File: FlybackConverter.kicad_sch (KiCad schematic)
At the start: 42 parts, among them J1 USB_C_Receptacle_PowerOnly_6P, T1 Transformer_1P_2S, U1 LNK6428K, U2 TPS25820DSST

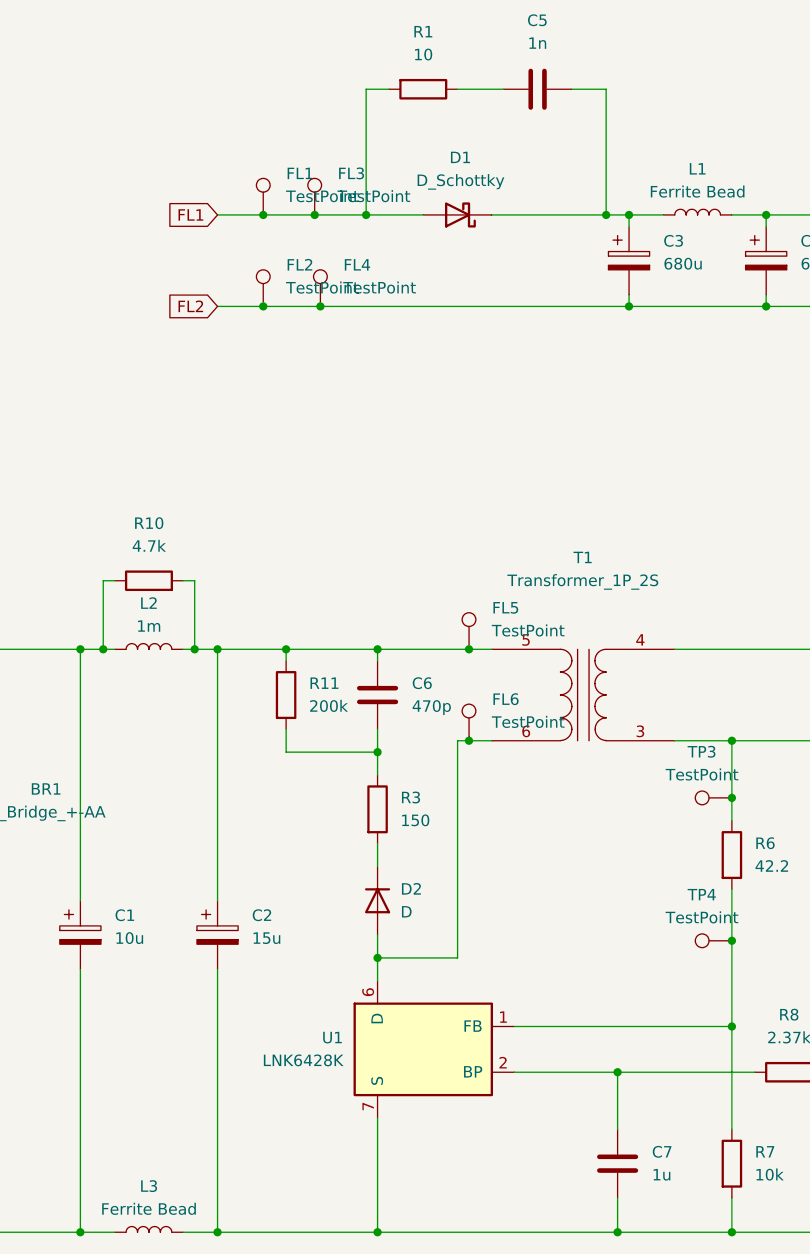
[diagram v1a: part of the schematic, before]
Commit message: トランスのフットプリントを10pinに修正
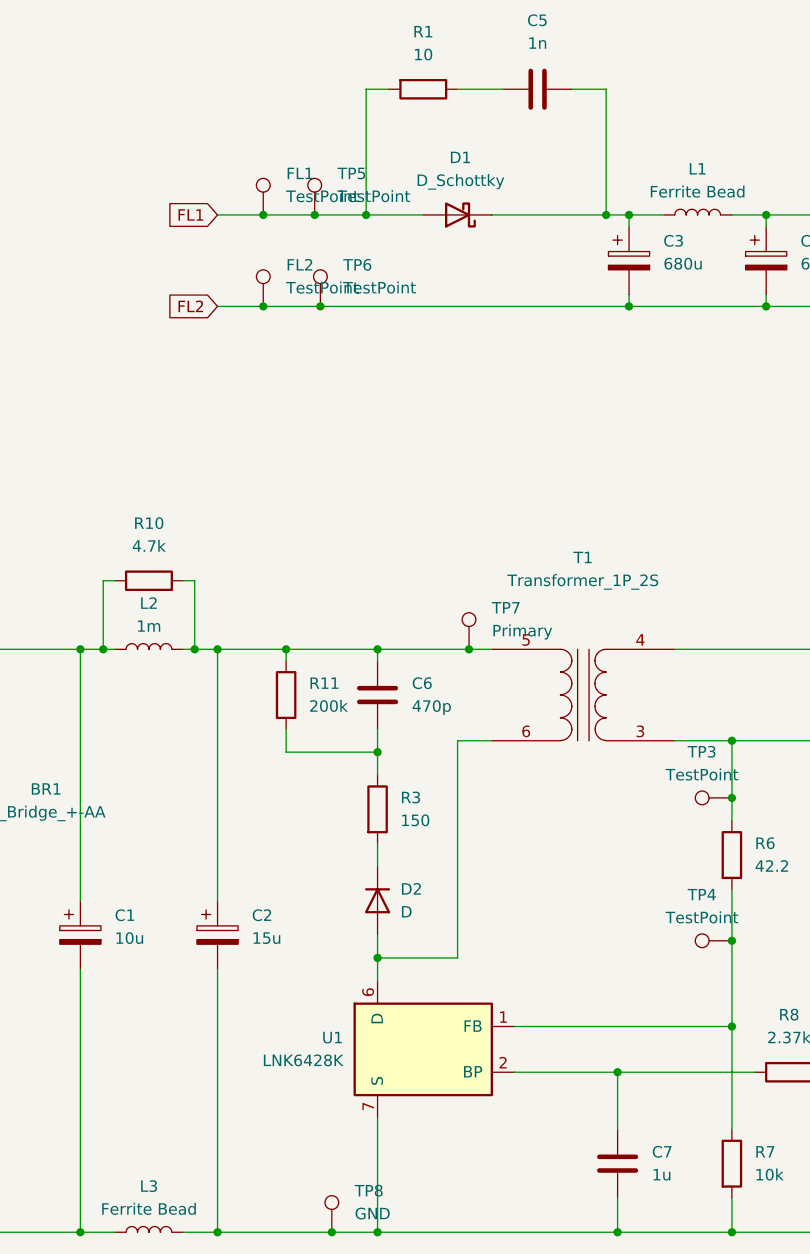
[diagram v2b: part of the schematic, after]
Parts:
- removed FL6: TestPoint, TestPoint:TestPoint_Loop_D1.80mm_Drill1.0mm_Beaded, symbol Connector:TestPoint
- added TP8: GND, TestPoint:TestPoint_Loop_D1.80mm_Drill1.0mm_Beaded, symbol Connector:TestPoint
- T1: footprint Transformer_THT:Transformer_CHK_EI38-3VA_2xSec -> 00_Library:BEPC17-1110CPHFR
- TP7: renamed from FL5; value TestPoint -> Primary
- renumbered FL3 to TP5, FL4 to TP6
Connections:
- net at C2.2, C7.2, C8.2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: now also TP8.1
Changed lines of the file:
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@@
   (junction (at 67.31 96.52) (diameter 0) (color 0 0 0 0)
   )
-  (junction (at 107.95 106.68) (diameter 0) (color 0 0 0 0)
-  )
   (junction (at 124.46 161.29) (diameter 0) (color 0 0 0 0)
   )
@@
   (junction (at 168.91 46.99) (diameter 0) (color 0 0 0 0)
   )
+  (junction (at 92.71 161.29) (diameter 0) (color 0 0 0 0)
+  )
   (junction (at 80.01 96.52) (diameter 0) (color 0 0 0 0)
   )
@@
     (stroke (width 0) (type default))
   )
-  (wire (pts (xy 106.68 106.68) (xy 107.95 106.68))
-    (stroke (width 0) (type default))
-  )
   (wire (pts (xy 97.79 105.41) (xy 97.79 107.95))
     (stroke (width 0) (type default))
@@
     (stroke (width 0) (type default))
   )
+  (wire (pts (xy 92.71 161.29) (xy 97.79 161.29))
+    (stroke (width 0) (type default))
+  )
   (wire (pts (xy 46.99 161.29) (xy 64.77 161.29))
     (stroke (width 0) (type default))
@@
     (stroke (width 0) (type default))
   )
-  (wire (pts (xy 107.95 106.68) (xy 110.49 106.68))
+  (wire (pts (xy 106.68 106.68) (xy 110.49 106.68))
     (stroke (width 0) (type default))
   )
@@
     (stroke (width 0) (type default))
   )
-  (wire (pts (xy 80.01 161.29) (xy 97.79 161.29))
+  (wire (pts (xy 80.01 161.29) (xy 92.71 161.29))
     (stroke (width 0) (type default))
   )
@@
     )
   )
-  (symbol (lib_id "Connector:TestPoint") (at 107.95 106.68 0) (unit 1)
-    (in_bom yes) (on_board yes) (dnp no) (fields_autoplaced)
-    (property "Reference" "FL6" (at 110.49 102.108 0)
-      (effects (font (size 1.27 1.27)) (justify left))
-    )
-    (property "Value" "TestPoint" (at 110.49 104.648 0)
-      (effects (font (size 1.27 1.27)) (justify left))
-    )
-    (property "Footprint" "TestPoint:TestPoint_Loop_D1.80mm_Drill1.0mm_Beaded" (at 113.03 106.68 0)
-      (effects (font (size 1.27 1.27)) hide)
-    )
-    (property "Datasheet" "~" (at 113.03 106.68 0)
-      (effects (font (size 1.27 1.27)) hide)
-    )
-    (pin "1")
-    (instances
-      (project "FlybackConverter"
-        (path "/f7ad8aa8-e3ae-4e7c-846c-9c0c6caa5ffd"
-          (reference "FL6") (unit 1)
-        )
-      )
-    )
-  )
   (symbol (lib_id "Device:R") (at 72.39 88.9 90) (unit 1)
     (in_bom yes) (on_board yes) (dnp no) (fields_autoplaced)
@@
     )
   )
+  (symbol (lib_id "Connector:TestPoint") (at 92.71 161.29 0) (unit 1)
+    (in_bom yes) (on_board yes) (dnp no) (fields_autoplaced)
+    (property "Reference" "TP8" (at 95.25 156.718 0)
+      (effects (font (size 1.27 1.27)) (justify left))
+    )
+    (property "Value" "GND" (at 95.25 159.258 0)
+      (effects (font (size 1.27 1.27)) (justify left))
+    )
+    (property "Footprint" "TestPoint:TestPoint_Loop_D1.80mm_Drill1.0mm_Beaded" (at 97.79 161.29 0)
+      (effects (font (size 1.27 1.27)) hide)
+    )
+    (property "Datasheet" "~" (at 97.79 161.29 0)
+      (effects (font (size 1.27 1.27)) hide)
+    )
+    (pin "1")
+    (instances
+      (project "FlybackConverter"
+        (path "/f7ad8aa8-e3ae-4e7c-846c-9c0c6caa5ffd"
+          (reference "TP8") (unit 1)
+        )
+      )
+    )
+  )
   (symbol (lib_id "Connector:TestPoint") (at 34.29 138.43 180) (unit 1)
     (in_bom yes) (on_board yes) (dnp no) (fields_autoplaced)
@@
   (symbol (lib_id "Connector:TestPoint") (at 90.805 48.26 0) (unit 1)
     (in_bom yes) (on_board yes) (dnp no) (fields_autoplaced)
-    (property "Reference" "FL3" (at 93.345 43.688 0)
+    (property "Reference" "TP5" (at 93.345 43.688 0)
       (effects (font (size 1.27 1.27)) (justify left))
     )
@@
       (project "FlybackConverter"
         (path "/f7ad8aa8-e3ae-4e7c-846c-9c0c6caa5ffd"
-          (reference "FL3") (unit 1)
+          (reference "TP5") (unit 1)
         )
       )
@@
       (effects (font (size 1.27 1.27)))
     )
-    (property "Footprint" "Transformer_THT:Transformer_CHK_EI38-3VA_2xSec" (at 120.65 101.6 0)
+    (property "Footprint" "00_Library:BEPC17-1110CPHFR" (at 120.65 101.6 0)
       (effects (font (size 1.27 1.27)) hide)
     )
@@
   (symbol (lib_id "Connector:TestPoint") (at 91.44 58.42 0) (unit 1)
     (in_bom yes) (on_board yes) (dnp no) (fields_autoplaced)
-    (property "Reference" "FL4" (at 93.98 53.848 0)
+    (property "Reference" "TP6" (at 93.98 53.848 0)
       (effects (font (size 1.27 1.27)) (justify left))
     )
@@
       (project "FlybackConverter"
         (path "/f7ad8aa8-e3ae-4e7c-846c-9c0c6caa5ffd"
-          (reference "FL4") (unit 1)
+          (reference "TP6") (unit 1)
         )
       )
@@
   (symbol (lib_id "Connector:TestPoint") (at 107.95 96.52 0) (unit 1)
     (in_bom yes) (on_board yes) (dnp no) (fields_autoplaced)
-    (property "Reference" "FL5" (at 110.49 91.948 0)
-      (effects (font (size 1.27 1.27)) (justify left))
-    )
-    (property "Value" "TestPoint" (at 110.49 94.488 0)
+    (property "Reference" "TP7" (at 110.49 91.948 0)
+      (effects (font (size 1.27 1.27)) (justify left))
+    )
+    (property "Value" "Primary" (at 110.49 94.488 0)
       (effects (font (size 1.27 1.27)) (justify left))
     )
@@
       (project "FlybackConverter"
         (path "/f7ad8aa8-e3ae-4e7c-846c-9c0c6caa5ffd"
-          (reference "FL5") (unit 1)
-        )
-      )
+          (reference "TP7") (unit 1)
+        )
+      )

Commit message: C7のフットプリントを1206に変更 #5
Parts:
- C7: footprint Capacitor_SMD:C_0805_2012Metric -> Capacitor_SMD:C_1206_3216Metric
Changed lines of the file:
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@@
       (effects (font (size 1.27 1.27)) (justify left))
     )
-    (property "Footprint" "Capacitor_SMD:C_0805_2012Metric" (at 125.4252 157.48 0)
+    (property "Footprint" "Capacitor_SMD:C_1206_3216Metric" (at 125.4252 157.48 0)
       (effects (font (size 1.27 1.27)) hide)
     )

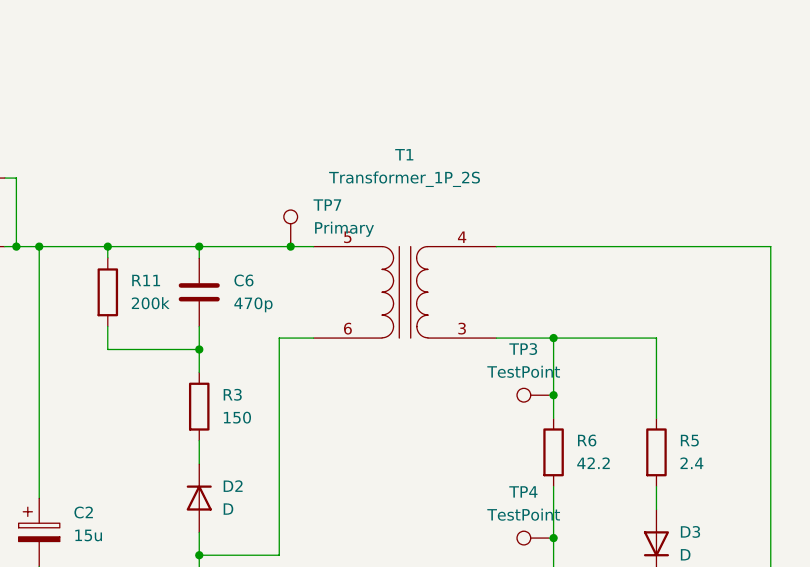
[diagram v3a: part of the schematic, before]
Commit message: トランスのフットプリント修正、それに合わせて部品配置も調整 fix #6
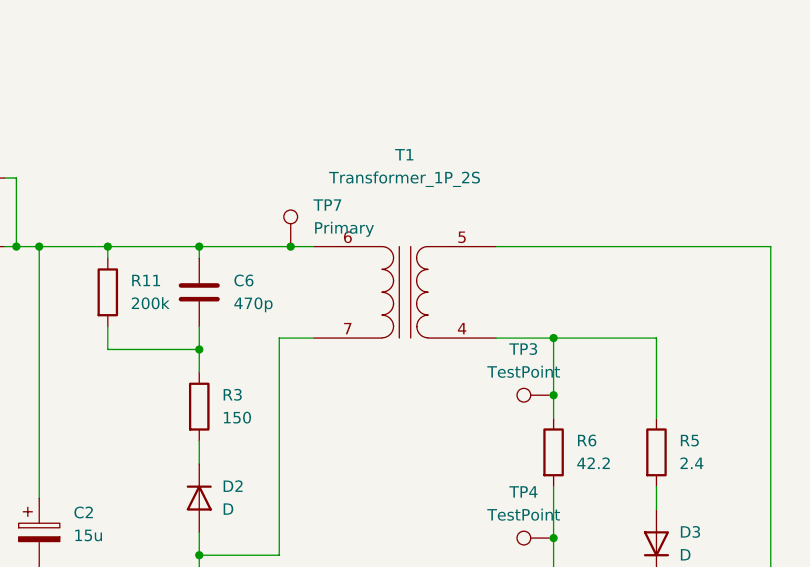
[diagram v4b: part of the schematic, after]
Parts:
- T1: footprint 00_Library:BEPC17-1110CPHFR -> 00_Library:B66206W1110T001
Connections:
- net at C2.1, C6.1, L2.2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: now also T1.6 (AA); no longer T1.5 (AA)
- net at C2.2, C7.2, C8.2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: now also T1.5 (SB); no longer T1.4 (SB)
- net at D2.2 (A), U1.6 (D): now also T1.7 (AB); no longer T1.6 (AB)
- net at R5.1, R6.1, TP3.1: now also T1.4 (SA); no longer T1.3 (SA)
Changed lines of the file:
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@@
       (effects (font (size 1.27 1.27)))
     )
-    (property "Footprint" "00_Library:BEPC17-1110CPHFR" (at 120.65 101.6 0)
+    (property "Footprint" "00_Library:B66206W1110T001" (at 120.65 101.6 0)
       (effects (font (size 1.27 1.27)) hide)
     )
@@
       (effects (font (size 1.27 1.27)) hide)
     )
-    (pin "3")
     (pin "4")
     (pin "5")
     (pin "6")
+    (pin "7")
     (instances
       (project "FlybackConverter"

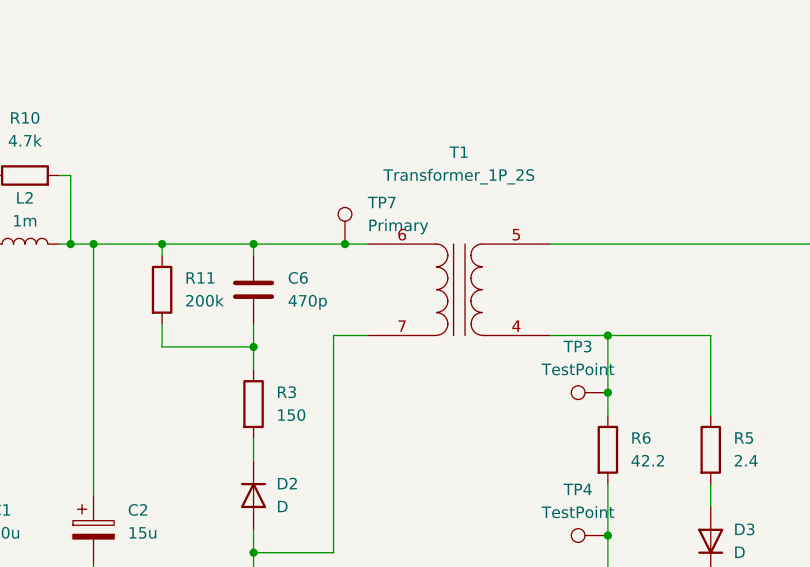
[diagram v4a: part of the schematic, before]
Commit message: トランス周辺のネット名変更
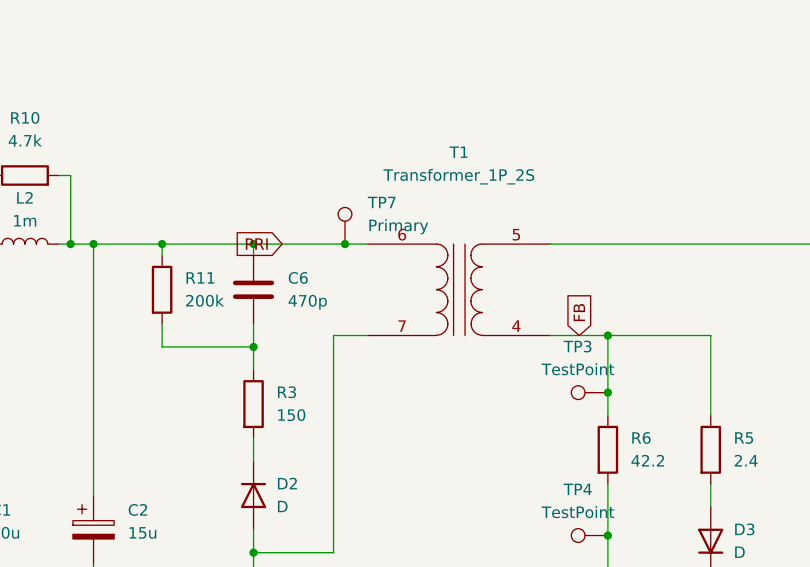
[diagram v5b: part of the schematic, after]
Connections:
- net PRI: now reaches C2.1, C6.1, L2.2, R10.2, R11.1, T1.6 (AA), TP7.1
- net FB: now reaches R5.1, R6.1, T1.4 (SA), TP3.1
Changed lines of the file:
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@@
+    )
+  )
+  (global_label "PRI" (shape input) (at 100.965 96.52 180) (fields_autoplaced)
+    (effects (font (size 1.27 1.27)) (justify right))
+    (property "Intersheetrefs" "${INTERSHEET_REFS}" (at 94.835 96.52 0)
+      (effects (font (size 1.27 1.27)) (justify right) hide)
     )
   )
@@
       (effects (font (size 1.27 1.27)) (justify left) hide)
     )
+  )
+  (global_label "FB" (shape input) (at 133.985 106.68 90) (fields_autoplaced)
+    (effects (font (size 1.27 1.27)) (justify left))
+    (property "Intersheetrefs" "${INTERSHEET_REFS}" (at 133.985 101.3362 90)
+      (effects (font (size 1.27 1.27)) (justify left) hide)
+    )
